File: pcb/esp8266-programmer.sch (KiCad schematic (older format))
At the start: 9 parts, among them P1 USB_OTG, P2 CONN_01X04, SW1 RESET, SW2 FLASH, SW3 SW_DP3T, U1 AP1117

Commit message: Edit Kicad schematic to add basic components
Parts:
- added JP1: Jumper_NO_Dual, symbol Jumper_NO_Dual
- added R1, R2, R3, R?: R, symbol R
- gave numbers to parts that had none: 1
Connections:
- net labels added: PP_CH_EN, PP_GPIO0, PP_GPIO15, PP_GPIO2, PP_REST, VCC
- wire segments 18 -> 32
- no-connect marks 2 -> 3
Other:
- moved on the sheet: SW1, SW2, SW3B
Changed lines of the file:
@@
 LIBS:switches
 LIBS:sw_dp3t
+LIBS:jumper_no_dual
 LIBS:esp8266-programmer-cache
 EELAYER 25 0
@@
 L SW_Push_Dual SW2
 U 1 1 58DAC3C7
-P 4450 3450
-F 0 "SW2" H 4500 3550 50  0000 L CNN
-F 1 "FLASH" H 4450 3180 50  0000 C CNN
-F 2 "" H 4450 3650 50  0000 C CNN
-F 3 "" H 4450 3650 50  0000 C CNN
-	1    4450 3450
-	1    0    0    -1
+P 3650 3050
+F 0 "SW2" H 3700 3150 50  0000 L CNN
+F 1 "FLASH" H 3650 2780 50  0000 C CNN
+F 2 "" H 3650 3250 50  0000 C CNN
+F 3 "" H 3650 3250 50  0000 C CNN
+	1    3650 3050
+	-1   0    0    -1
 $EndComp
 $Comp
 L SW_Push_Dual SW1
 U 1 1 58DAC45A
-P 4450 2750
-F 0 "SW1" H 4500 2850 50  0000 L CNN
-F 1 "RESET" H 4450 2480 50  0000 C CNN
-F 2 "" H 4450 2950 50  0000 C CNN
-F 3 "" H 4450 2950 50  0000 C CNN
-	1    4450 2750
+P 1300 1650
+F 0 "SW1" H 1350 1750 50  0000 L CNN
+F 1 "RESET" H 1300 1380 50  0000 C CNN
+F 2 "" H 1300 1850 50  0000 C CNN
+F 3 "" H 1300 1850 50  0000 C CNN
+	1    1300 1650
 	1    0    0    -1
 $EndComp
@@
 NoConn ~ 8850 2450
 $Comp
-L SW_DP3T SW?
+L SW_DP3T SW3
 U 2 1 58DC1770
-P 5800 2550
-F 0 "SW?" H 5800 2750 50  0000 C CNN
-F 1 "SW_DP3T" H 5800 2350 50  0000 C CNN
-F 2 "" H 5175 2725 50  0000 C CNN
-F 3 "" H 5175 2725 50  0000 C CNN
-	2    5800 2550
+P 5800 2050
+F 0 "SW3" H 5800 2250 50  0000 C CNN
+F 1 "SW_DP3T" H 5800 1850 50  0000 C CNN
+F 2 "" H 5175 2225 50  0000 C CNN
+F 3 "" H 5175 2225 50  0000 C CNN
+	2    5800 2050
 	1    0    0    -1
 $EndComp
@@
 	8550 2650 6000 2650
 Wire Wire Line
-	6000 2050 6350 2050
+	6000 1950 6350 1950
 Wire Wire Line
 	6650 2350 7150 2350
 Wire Wire Line
-	6000 2050 6000 2550
-Connection ~ 6000 2450
-Wire Wire Line
-	5600 2550 5600 2050
-Wire Wire Line
-	5600 2050 5300 2050
+	5050 2050 5600 2050
 $Comp
 L GND #PWR?
@@
 Wire Wire Line
 	5300 2350 5300 2400
+Wire Wire Line
+	6000 2650 6000 2150
+Wire Wire Line
+	6000 1950 6000 2050
+Connection ~ 6000 1950
+Wire Wire Line
+	6350 1950 6350 2050
+Connection ~ 5300 2050
+$Comp
+L VCC #PWR?
+U 1 1 58DECEB5
+P 5050 2050
+F 0 "#PWR?" H 5050 1900 50  0001 C CNN
+F 1 "VCC" H 5050 2200 50  0000 C CNN
+F 2 "" H 5050 2050 50  0000 C CNN
+F 3 "" H 5050 2050 50  0000 C CNN
+	1    5050 2050
+	1    0    0    -1
+$EndComp
+Wire Wire Line
+	1100 1500 1100 1850
+Connection ~ 1100 1650
+$Comp
+L R R1
+U 1 1 58DED73E
+P 1100 1350
+F 0 "R1" H 1200 1350 50  0000 C CNN
+F 1 "R" H 1100 1350 50  0000 C CNN
+F 2 "" V 1030 1350 50  0000 C CNN
+F 3 "" H 1100 1350 50  0000 C CNN
+	1    1100 1350
+	1    0    0    -1
+$EndComp
+$Comp
+L VCC #PWR?
+U 1 1 58DED85C
+P 1100 1200
+F 0 "#PWR?" H 1100 1050 50  0001 C CNN
+F 1 "VCC" H 1100 1350 50  0000 C CNN
+F 2 "" H 1100 1200 50  0000 C CNN
+F 3 "" H 1100 1200 50  0000 C CNN
+	1    1100 1200
+	1    0    0    -1
+$EndComp
+Wire Wire Line
+	1500 1650 1500 1850
+Wire Wire Line
+	1500 1850 1950 1850
+Connection ~ 1500 1850
+Text Label 1800 1800 0    60   ~ 0
+PP_REST
+Wire Wire Line
+	3850 2900 3850 3250
+Connection ~ 3850 3050
+$Comp
+L R R3
+U 1 1 58DEDCA6
+P 3850 2750
+F 0 "R3" H 3950 2750 50  0000 C CNN
+F 1 "R" H 3850 2750 50  0000 C CNN
+F 2 "" V 3780 2750 50  0000 C CNN
+F 3 "" H 3850 2750 50  0000 C CNN
+	1    3850 2750
+	-1   0    0    -1
+$EndComp
+$Comp
+L VCC #PWR?
+U 1 1 58DEDE0F
+P 3850 2600
+F 0 "#PWR?" H 3850 2450 50  0001 C CNN
+F 1 "VCC" H 3850 2750 50  0000 C CNN
+F 2 "" H 3850 2600 50  0000 C CNN
+F 3 "" H 3850 2600 50  0000 C CNN
+	1    3850 2600
+	-1   0    0    -1
+$EndComp
+Wire Wire Line
+	3450 3050 3450 3250
+Wire Wire Line
+	3450 3250 3150 3250
+Connection ~ 3450 3250
+Text Label 3350 3200 2    60   ~ 0
+PP_GPIO0
+$Comp
+L VCC #PWR?
+U 1 1 58DEDF75
+P 1100 2800
+F 0 "#PWR?" H 1100 2650 50  0001 C CNN
+F 1 "VCC" H 1100 2950 50  0000 C CNN
+F 2 "" H 1100 2800 50  0000 C CNN
+F 3 "" H 1100 2800 50  0000 C CNN
+	1    1100 2800
+	1    0    0    -1
+$EndComp
+$Comp
+L R R2
+U 1 1 58DEDF9F
+P 1100 2950
+F 0 "R2" H 1200 2950 50  0000 C CNN
+F 1 "R" H 1100 2950 50  0000 C CNN
+F 2 "" V 1030 2950 50  0000 C CNN
+F 3 "" H 1100 2950 50  0000 C CNN
+	1    1100 2950
+	1    0    0    -1
+$EndComp
+Wire Wire Line
+	1100 3100 1100 3250
+Wire Wire Line
+	1100 3250 1950 3250
+Text Label 1750 3200 0    60   ~ 0
+PP_CH_EN
+$Comp
+L VCC #PWR?
+U 1 1 58DEEB71
+P 3850 4050
+F 0 "#PWR?" H 3850 3900 50  0001 C CNN
+F 1 "VCC" H 3850 4200 50  0000 C CNN
+F 2 "" H 3850 4050 50  0000 C CNN
+F 3 "" H 3850 4050 50  0000 C CNN
+	1    3850 4050
+	-1   0    0    -1
+$EndComp
+$Comp
+L R R?
+U 1 1 58DEEB77
+P 3850 4200
+F 0 "R?" V 3930 4200 50  0000 C CNN
+F 1 "R" V 3850 4200 50  0000 C CNN
+F 2 "" V 3780 4200 50  0000 C CNN
+F 3 "" H 3850 4200 50  0000 C CNN
+	1    3850 4200
+	-1   0    0    -1
+$EndComp
+Wire Wire Line
+	3850 4350 3850 4500
+Wire Wire Line
+	3850 4500 3150 4500
+Text Label 3350 4450 2    60   ~ 0
+PP_GPIO2
+$Comp
+L Jumper_NO_Dual JP1
+U 1 1 58DEE706
+P 1600 2100
+F 0 "JP1" V 1700 1850 50  0000 L CNN
+F 1 "Jumper_NO_Dual" V 1700 2550 50  0000 C BNN
+F 2 "" H 1600 2100 50  0000 C CNN
+F 3 "" H 1600 2100 50  0000 C CNN
+	1    1600 2100
+	0    -1   1    0
+$EndComp
+Wire Wire Line
+	1700 2100 1950 2100
+Text Label 1800 2050 0    60   ~ 0
+PP_REST
+NoConn ~ 1600 2350
+Wire Wire Line
+	3150 4850 3850 4850
+Wire Wire Line
+	3850 4850 3850 4950
+$Comp
+L GND #PWR?
+U 1 1 58DEF6C2
+P 3850 4950
+F 0 "#PWR?" H 3850 4700 50  0001 C CNN
+F 1 "GND" H 3850 4800 50  0000 C CNN
+F 2 "" H 3850 4950 50  0000 C CNN
+F 3 "" H 3850 4950 50  0000 C CNN
+	1    3850 4950
+	1    0    0    -1
+$EndComp
+Text Label 3350 4800 2    60   ~ 0
+PP_GPIO15
 $EndSCHEMATC

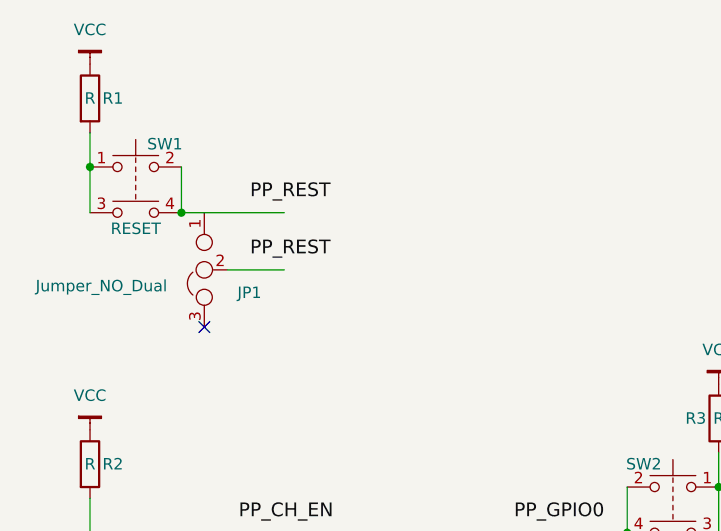
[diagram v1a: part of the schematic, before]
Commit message: Edit Kicad schematic to add basic components (again)
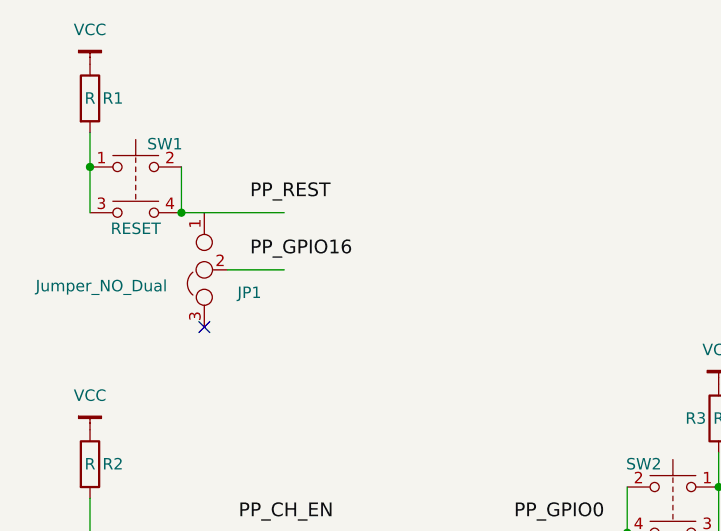
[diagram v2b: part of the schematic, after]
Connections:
- net labels added: PP_GPIO16
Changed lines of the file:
@@
 	1700 2100 1950 2100
 Text Label 1800 2050 0    60   ~ 0
-PP_REST
+PP_GPIO16
 NoConn ~ 1600 2350
 Wire Wire Line

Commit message: Add ESP chip, USB chip and some pin designations
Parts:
- added U?: ESP-12, symbol ESP-12
- added U?: MCP2221-I/SL, IPC7351-Nominal:SOIC127P600X175-14, symbol MCP2221-I/SL
- P1: symbol USB_OTG -> USB_OTG-RESCUE-esp8266-programmer
- U1: symbol AP1117 -> AP1117-RESCUE-esp8266-programmer
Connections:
- net labels added: D+, D-, PP_ADC, PP_GPIO12, PP_GPIO13, PP_GPIO14, PP_GPIO4, PP_GPIO5, PP_RXD, PP_TXD
- wire segments 32 -> 53
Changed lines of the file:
@@
 EESchema Schematic File Version 2
+LIBS:esp8266-programmer-rescue
 LIBS:power
 LIBS:device
@@
 LIBS:valves
 LIBS:switches
-LIBS:sw_dp3t
-LIBS:jumper_no_dual
+LIBS:ESP8266
+LIBS:Microchip
 LIBS:esp8266-programmer-cache
 EELAYER 25 0
@@
 $EndDescr
 $Comp
-L USB_OTG P1
+L USB_OTG-RESCUE-esp8266-programmer P1
 U 1 1 58DABF08
 P 9150 1650
@@
 $EndComp
 $Comp
-L AP1117 U1
+L AP1117-RESCUE-esp8266-programmer U1
 U 1 1 58DC158E
 P 6650 2050
@@
 Text Label 3350 4800 2    60   ~ 0
 PP_GPIO15
+$Comp
+L ESP-12 U?
+U 1 1 58DFBEBA
+P 6450 4200
+F 0 "U?" H 6450 4100 50  0000 C CNN
+F 1 "ESP-12" H 6450 4300 50  0000 C CNN
+F 2 "" H 6450 4200 50  0001 C CNN
+F 3 "" H 6450 4200 50  0001 C CNN
+	1    6450 4200
+	1    0    0    -1
+$EndComp
+Wire Wire Line
+	5550 3900 5100 3900
+Text Label 5150 3900 0    60   ~ 0
+PP_REST
+Wire Wire Line
+	5550 4100 5100 4100
+Text Label 5150 4100 0    60   ~ 0
+PP_CH_EN
+Wire Wire Line
+	5550 4000 5100 4000
+Text Label 5150 4000 0    60   ~ 0
+PP_ADC
+Wire Wire Line
+	5550 4200 5100 4200
+Text Label 5150 4200 0    60   ~ 0
+PP_GPIO16
+Wire Wire Line
+	5550 4300 5100 4300
+Text Label 5150 4300 0    60   ~ 0
+PP_GPIO14
+Wire Wire Line
+	5550 4400 5100 4400
+Text Label 5150 4400 0    60   ~ 0
+PP_GPIO12
+Wire Wire Line
+	5550 4500 5100 4500
+Text Label 5150 4500 0    60   ~ 0
+PP_GPIO13
+Wire Wire Line
+	7350 4500 7800 4500
+Wire Wire Line
+	7350 4400 7800 4400
+Wire Wire Line
+	7350 4300 7800 4300
+Wire Wire Line
+	7350 4200 7800 4200
+Wire Wire Line
+	7350 4100 7800 4100
+Wire Wire Line
+	7350 4000 7800 4000
+Wire Wire Line
+	7350 3900 7800 3900
+Text Label 7300 3900 0    60   ~ 0
+PP_TXD
+Text Label 7300 4000 0    60   ~ 0
+PP_RXD
+Text Label 7300 4100 0    60   ~ 0
+PP_GPIO5
+Text Label 7300 4200 0    60   ~ 0
+PP_GPIO4
+Text Label 7300 4300 0    60   ~ 0
+PP_GPIO0
+Text Label 7300 4400 0    60   ~ 0
+PP_GPIO2
+Text Label 7300 4500 0    60   ~ 0
+PP_GPIO15
+$Comp
+L MCP2221-I/SL U?
+U 1 1 58DFCE15
+P 9150 4250
+F 0 "U?" H 9150 5100 50  0000 C CNN
+F 1 "MCP2221-I/SL" H 9150 5000 50  0000 C CNN
+F 2 "IPC7351-Nominal:SOIC127P600X175-14" H 9150 5000 60  0001 C CNN
+F 3 "http://ww1.microchip.com/downloads/en/DeviceDoc/20005292B.pdf" H 9150 5000 60  0001 C CNN
+F 4 "IC MICROCHIP MCP2221-I/SL" H 9650 5800 60  0001 C CNN "BOM"
+	1    9150 4250
+	1    0    0    -1
+$EndComp
+Wire Wire Line
+	8550 3650 8450 3650
+Wire Wire Line
+	8450 3650 8450 3350
+$Comp
+L VCC #PWR?
+U 1 1 58DFD4A9
+P 8450 3350
+F 0 "#PWR?" H 8450 3400 30  0001 C CNN
+F 1 "VCC" H 8450 3450 50  0000 C CNN
+F 2 "" H 8450 3350 60  0000 C CNN
+F 3 "" H 8450 3350 60  0000 C CNN
+	1    8450 3350
+	1    0    0    -1
+$EndComp
+$Comp
+L VCC #PWR?
+U 1 1 58DFD4DD
+P 6450 3300
+F 0 "#PWR?" H 6450 3350 30  0001 C CNN
+F 1 "VCC" H 6450 3400 50  0000 C CNN
+F 2 "" H 6450 3300 60  0000 C CNN
+F 3 "" H 6450 3300 60  0000 C CNN
+	1    6450 3300
+	1    0    0    -1
+$EndComp
+$Comp
+L GND #PWR?
+U 1 1 58DFD60B
+P 8550 5350
+F 0 "#PWR?" H 8550 5350 30  0001 C CNN
+F 1 "GND" H 8550 5280 30  0001 C CNN
+F 2 "" H 8550 5350 60  0000 C CNN
+F 3 "" H 8550 5350 60  0000 C CNN
+	1    8550 5350
+	1    0    0    -1
+$EndComp
+Wire Wire Line
+	8550 4850 8550 5350
+Wire Wire Line
+	8850 1550 8500 1550
+Wire Wire Line
+	8850 1650 8500 1650
+Text Label 8600 1550 0    60   ~ 0
+D-
+Text Label 8600 1650 0    60   ~ 0
+D+
+Wire Wire Line
+	8550 4150 8400 4150
+Wire Wire Line
+	8550 4250 8400 4250
+Text Label 8450 4250 0    60   ~ 0
+D+
+Text Label 8450 4150 0    60   ~ 0
+D-
 $EndSCHEMATC

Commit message: Add custom Kicad libs directory to project directory
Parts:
- removed U1: AP1117, TO_SOT_Packages_SMD:SOT-223, symbol AP1117-RESCUE-esp8266-programmer
- added U1: MCP1700T-3302E/TT, KiCad/TO_SOT_Packages_SMD.pretty:SOT-23, symbol MCP1700T-3302E/TT
- gave numbers to parts that had none: 2
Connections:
- wire segments 53 -> 50
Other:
- moved on the sheet: C2, SW3B
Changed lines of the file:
@@
 LIBS:valves
 LIBS:switches
-LIBS:ESP8266
-LIBS:Microchip
+LIBS:mcp1700
+LIBS:jumper_no_dual
 LIBS:esp8266-programmer-cache
 EELAYER 25 0
@@
 $EndDescr
 $Comp
-L USB_OTG-RESCUE-esp8266-programmer P1
-U 1 1 58DABF08
-P 9150 1650
-F 0 "P1" V 8800 1650 50  0000 C CNN
-F 1 "USB_OTG" V 9150 2050 50  0000 C CNN
-F 2 "" V 9100 1550 50  0000 C CNN
-F 3 "" V 9100 1550 50  0000 C CNN
-	1    9150 1650
-	0    1    1    0
-$EndComp
-$Comp
 L SW_Push_Dual SW2
 U 1 1 58DAC3C7
@@
 $EndComp
 $Comp
-L GND #PWR01
-U 1 1 58DACFCE
-P 8850 1900
-F 0 "#PWR01" H 8850 1650 50  0001 C CNN
-F 1 "GND" H 8850 1750 50  0000 C CNN
-F 2 "" H 8850 1900 50  0000 C CNN
-F 3 "" H 8850 1900 50  0000 C CNN
-	1    8850 1900
-	1    0    0    -1
-$EndComp
-$Comp
-L GND #PWR02
-U 1 1 58DACFEE
-P 8850 2600
-F 0 "#PWR02" H 8850 2350 50  0001 C CNN
-F 1 "GND" H 8850 2450 50  0000 C CNN
-F 2 "" H 8850 2600 50  0000 C CNN
-F 3 "" H 8850 2600 50  0000 C CNN
-	1    8850 2600
-	1    0    0    -1
-$EndComp
-$Comp
 L SW_DP3T SW3
 U 1 1 58DC0605
 P 7650 2050
 F 0 "SW3" H 7650 2250 50  0000 C CNN
-F 1 "SW_DP3T" H 7650 1850 50  0000 C CNN
+F 1 "SW_DP3T" H 7600 1850 50  0000 C CNN
 F 2 "" H 7025 2225 50  0000 C CNN
 F 3 "" H 7025 2225 50  0000 C CNN
@@
 L CP C2
 U 1 1 58DC1487
-P 5300 2200
-F 0 "C2" H 5325 2300 50  0000 L CNN
-F 1 "CP" H 5325 2100 50  0000 L CNN
-F 2 "" H 5338 2050 50  0000 C CNN
-F 3 "" H 5300 2200 50  0000 C CNN
-	1    5300 2200
-	1    0    0    -1
-$EndComp
-$Comp
-L AP1117-RESCUE-esp8266-programmer U1
-U 1 1 58DC158E
-P 6650 2050
-F 0 "U1" H 6950 2250 50  0000 C CNN
-F 1 "AP1117" H 6650 2300 50  0000 C CNN
-F 2 "TO_SOT_Packages_SMD:SOT-223" H 6650 1700 50  0001 C CNN
-F 3 "" H 6750 1800 50  0000 C CNN
-	1    6650 2050
-	-1   0    0    -1
+P 5300 2300
+F 0 "C2" H 5325 2400 50  0000 L CNN
+F 1 "CP" H 5325 2200 50  0000 L CNN
+F 2 "" H 5338 2150 50  0000 C CNN
+F 3 "" H 5300 2300 50  0000 C CNN
+	1    5300 2300
+	1    0    0    -1
 $EndComp
 NoConn ~ 7850 2150
@@
 L SW_DP3T SW3
 U 2 1 58DC1770
-P 5800 2050
-F 0 "SW3" H 5800 2250 50  0000 C CNN
-F 1 "SW_DP3T" H 5800 1850 50  0000 C CNN
-F 2 "" H 5175 2225 50  0000 C CNN
-F 3 "" H 5175 2225 50  0000 C CNN
-	2    5800 2050
-	1    0    0    -1
-$EndComp
-$Comp
-L GND #PWR?
-U 1 1 58DC1DFC
-P 6900 2350
-F 0 "#PWR?" H 6900 2100 50  0001 C CNN
-F 1 "GND" H 6900 2200 50  0000 C CNN
-F 2 "" H 6900 2350 50  0000 C CNN
-F 3 "" H 6900 2350 50  0000 C CNN
-	1    6900 2350
+P 5800 2150
+F 0 "SW3" H 5800 2350 50  0000 C CNN
+F 1 "SW_DP3T" H 5750 1950 50  0000 C CNN
+F 2 "" H 5175 2325 50  0000 C CNN
+F 3 "" H 5175 2325 50  0000 C CNN
+	2    5800 2150
 	1    0    0    -1
 $EndComp
 Wire Wire Line
 	8100 1450 8850 1450
-Wire Wire Line
-	8850 1850 8850 2050
-Wire Wire Line
-	8850 2550 8850 2700
 Wire Wire Line
 	8100 1450 8100 1950
@@
 	8550 2650 6000 2650
 Wire Wire Line
-	6000 1950 6350 1950
+	6000 2050 6350 2050
 Wire Wire Line
 	6650 2350 7150 2350
 Wire Wire Line
-	5050 2050 5600 2050
-$Comp
-L GND #PWR?
+	5050 2150 5600 2150
+$Comp
+L GND-RESCUE-esp8266-programmer #PWR?
 U 1 1 58DC270D
-P 5300 2400
-F 0 "#PWR?" H 5300 2150 50  0001 C CNN
-F 1 "GND" H 5300 2250 50  0000 C CNN
-F 2 "" H 5300 2400 50  0000 C CNN
-F 3 "" H 5300 2400 50  0000 C CNN
-	1    5300 2400
-	1    0    0    -1
-$EndComp
-Wire Wire Line
-	5300 2350 5300 2400
-Wire Wire Line
-	6000 2650 6000 2150
-Wire Wire Line
-	6000 1950 6000 2050
-Connection ~ 6000 1950
-Wire Wire Line
-	6350 1950 6350 2050
-Connection ~ 5300 2050
-$Comp
-L VCC #PWR?
-U 1 1 58DECEB5
-P 5050 2050
-F 0 "#PWR?" H 5050 1900 50  0001 C CNN
-F 1 "VCC" H 5050 2200 50  0000 C CNN
-F 2 "" H 5050 2050 50  0000 C CNN
-F 3 "" H 5050 2050 50  0000 C CNN
-	1    5050 2050
-	1    0    0    -1
-$EndComp
+P 5300 2500
+F 0 "#PWR?" H 5300 2250 50  0001 C CNN
+F 1 "GND" H 5300 2400 50  0000 C CNN
+F 2 "" H 5300 2500 50  0000 C CNN
+F 3 "" H 5300 2500 50  0000 C CNN
+	1    5300 2500
+	1    0    0    -1
+$EndComp
+Wire Wire Line
+	5300 2450 5300 2500
+Wire Wire Line
+	6000 2650 6000 2250
+Wire Wire Line
+	6000 2050 6000 2150
+Connection ~ 6000 2050
+Connection ~ 5300 2150
 Wire Wire Line
 	1100 1500 1100 1850
@@
 $EndComp
 $Comp
-L R R?
+L R R4
 U 1 1 58DEEB77
 P 3850 4200
-F 0 "R?" V 3930 4200 50  0000 C CNN
-F 1 "R" V 3850 4200 50  0000 C CNN
+F 0 "R4" H 3950 4200 50  0000 C CNN
+F 1 "R" H 3850 4200 50  0000 C CNN
 F 2 "" V 3780 4200 50  0000 C CNN
 F 3 "" H 3850 4200 50  0000 C CNN
@@
 	3850 4850 3850 4950
 $Comp
-L GND #PWR?
+L GND-RESCUE-esp8266-programmer #PWR?
 U 1 1 58DEF6C2
 P 3850 4950
 F 0 "#PWR?" H 3850 4700 50  0001 C CNN
-F 1 "GND" H 3850 4800 50  0000 C CNN
+F 1 "GND" H 3850 4850 50  0000 C CNN
 F 2 "" H 3850 4950 50  0000 C CNN
 F 3 "" H 3850 4950 50  0000 C CNN
@@
 PP_GPIO15
 $Comp
-L MCP2221-I/SL U?
+L MCP2221-I/SL U1
 U 1 1 58DFCE15
 P 9150 4250
-F 0 "U?" H 9150 5100 50  0000 C CNN
+F 0 "U1" H 9150 5100 50  0000 C CNN
 F 1 "MCP2221-I/SL" H 9150 5000 50  0000 C CNN
 F 2 "IPC7351-Nominal:SOIC127P600X175-14" H 9150 5000 60  0001 C CNN
@@
 $EndComp
 Wire Wire Line
-	8550 3650 8450 3650
-Wire Wire Line
-	8450 3650 8450 3350
-$Comp
-L VCC #PWR?
-U 1 1 58DFD4A9
-P 8450 3350
-F 0 "#PWR?" H 8450 3400 30  0001 C CNN
-F 1 "VCC" H 8450 3450 50  0000 C CNN
-F 2 "" H 8450 3350 60  0000 C CNN
-F 3 "" H 8450 3350 60  0000 C CNN
-	1    8450 3350
-	1    0    0    -1
-$EndComp
-$Comp
-L VCC #PWR?
-U 1 1 58DFD4DD
-P 6450 3300
-F 0 "#PWR?" H 6450 3350 30  0001 C CNN
-F 1 "VCC" H 6450 3400 50  0000 C CNN
-F 2 "" H 6450 3300 60  0000 C CNN
-F 3 "" H 6450 3300 60  0000 C CNN
-	1    6450 3300
-	1    0    0    -1
-$EndComp
-$Comp
-L GND #PWR?
-U 1 1 58DFD60B
-P 8550 5350
-F 0 "#PWR?" H 8550 5350 30  0001 C CNN
-F 1 "GND" H 8550 5280 30  0001 C CNN
-F 2 "" H 8550 5350 60  0000 C CNN
-F 3 "" H 8550 5350 60  0000 C CNN
-	1    8550 5350
-	1    0    0    -1
-$EndComp
-Wire Wire Line
-	8550 4850 8550 5350
+	8550 3650 8550 3350
 Wire Wire Line
 	8850 1550 8500 1550
@@
 Text Label 8450 4150 0    60   ~ 0
 D-
+$Comp
+L GND #PWR?
+U 1 1 58E05ABF
+P 6900 2350
+F 0 "#PWR?" H 6900 2100 50  0001 C CNN
+F 1 "GND" H 6900 2200 50  0000 C CNN
+F 2 "" H 6900 2350 50  0000 C CNN
+F 3 "" H 6900 2350 50  0000 C CNN
+	1    6900 2350
+	1    0    0    -1
+$EndComp
+Connection ~ 6900 2350
+$Comp
+L USB_OTG-RESCUE-esp8266-programmer P1
+U 1 1 58DABF08
+P 9150 1650
+F 0 "P1" V 8850 1650 50  0000 C CNN
+F 1 "USB_OTG" V 9150 2050 50  0000 C CNN
+F 2 "" V 9100 1550 50  0000 C CNN
+F 3 "" V 9100 1550 50  0000 C CNN
+	1    9150 1650
+	0    1    1    0
+$EndComp
+$Comp
+L GND #PWR?
+U 1 1 58E05F00
+P 8850 1850
+F 0 "#PWR?" H 8850 1600 50  0001 C CNN
+F 1 "GND" H 8850 1700 50  0000 C CNN
+F 2 "" H 8850 1850 50  0000 C CNN
+F 3 "" H 8850 1850 50  0000 C CNN
+	1    8850 1850
+	1    0    0    -1
+$EndComp
+$Comp
+L GND #PWR?
+U 1 1 58E05FC7
+P 8850 2550
+F 0 "#PWR?" H 8850 2300 50  0001 C CNN
+F 1 "GND" H 8850 2400 50  0000 C CNN
+F 2 "" H 8850 2550 50  0000 C CNN
+F 3 "" H 8850 2550 50  0000 C CNN
+	1    8850 2550
+	1    0    0    -1
+$EndComp
+$Comp
+L VCC #PWR?
+U 1 1 58E06460
+P 8550 3350
+F 0 "#PWR?" H 8550 3200 50  0001 C CNN
+F 1 "VCC" H 8550 3500 50  0000 C CNN
+F 2 "" H 8550 3350 50  0000 C CNN
+F 3 "" H 8550 3350 50  0000 C CNN
+	1    8550 3350
+	1    0    0    -1
+$EndComp
+$Comp
+L GND #PWR?
+U 1 1 58E064F7
+P 8550 5000
+F 0 "#PWR?" H 8550 4750 50  0001 C CNN
+F 1 "GND" H 8550 4850 50  0000 C CNN
+F 2 "" H 8550 5000 50  0000 C CNN
+F 3 "" H 8550 5000 50  0000 C CNN
+	1    8550 5000
+	1    0    0    -1
+$EndComp
+Wire Wire Line
+	8550 4850 8550 5000
+$Comp
+L VCC #PWR?
+U 1 1 58E066ED
+P 6450 3300
+F 0 "#PWR?" H 6450 3150 50  0001 C CNN
+F 1 "VCC" H 6450 3450 50  0000 C CNN
+F 2 "" H 6450 3300 50  0000 C CNN
+F 3 "" H 6450 3300 50  0000 C CNN
+	1    6450 3300
+	1    0    0    -1
+$EndComp
+$Comp
+L GND #PWR?
+U 1 1 58E067DB
+P 6450 5100
+F 0 "#PWR?" H 6450 4850 50  0001 C CNN
+F 1 "GND" H 6450 4950 50  0000 C CNN
+F 2 "" H 6450 5100 50  0000 C CNN
+F 3 "" H 6450 5100 50  0000 C CNN
+	1    6450 5100
+	1    0    0    -1
+$EndComp
+$Comp
+L VCC #PWR?
+U 1 1 58E06D8F
+P 5050 2050
+F 0 "#PWR?" H 5050 1900 50  0001 C CNN
+F 1 "VCC" H 5050 2200 50  0000 C CNN
+F 2 "" H 5050 2050 50  0000 C CNN
+F 3 "" H 5050 2050 50  0000 C CNN
+	1    5050 2050
+	1    0    0    -1
+$EndComp
+Wire Wire Line
+	5050 2050 5050 2150
+$Comp
+L MCP1700T-3302E/TT U1
+U 1 1 58E084E7
+P 6650 2150
+F 0 "U1" H 6750 1950 50  0000 C CNN
+F 1 "MCP1700T-3302E/TT" H 6650 2450 50  0000 C CNN
+F 2 "KiCad/TO_SOT_Packages_SMD.pretty:SOT-23" H 6650 2250 50  0001 C CNN
+F 3 "http://docs-europe.electrocomponents.com/webdocs/0dd1/0900766b80dd189b.pdf" H 6650 2250 50  0001 C CNN
+	1    6650 2150
+	-1   0    0    -1
+$EndComp
 $EndSCHEMATC

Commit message: Create kicad_extras directory for libs, modules, 3d shapes. Move relevant files. Set relative paths for libs
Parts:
- U?: footprint (none) -> jdunmire/kicad-ESP8266/ESP8266.pretty:ESP-12
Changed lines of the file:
@@
 EESchema Schematic File Version 2
-LIBS:esp8266-programmer-rescue
 LIBS:power
 LIBS:device
@@
 LIBS:valves
 LIBS:switches
+LIBS:ESP8266
+LIBS:Microchip
 LIBS:mcp1700
 LIBS:jumper_no_dual
@@
 F 0 "U?" H 6450 4100 50  0000 C CNN
 F 1 "ESP-12" H 6450 4300 50  0000 C CNN
-F 2 "" H 6450 4200 50  0001 C CNN
+F 2 "jdunmire/kicad-ESP8266/ESP8266.pretty:ESP-12" H 6450 4200 50  0001 C CNN
 F 3 "" H 6450 4200 50  0001 C CNN
 	1    6450 4200
@@
 D-
 $Comp
-L GND #PWR?
+L GND-RESCUE-esp8266-programmer #PWR?
 U 1 1 58E05ABF
 P 6900 2350
@@
 $EndComp
 $Comp
-L GND #PWR?
+L GND-RESCUE-esp8266-programmer #PWR?
 U 1 1 58E05F00
 P 8850 1850
@@
 $EndComp
 $Comp
-L GND #PWR?
+L GND-RESCUE-esp8266-programmer #PWR?
 U 1 1 58E05FC7
 P 8850 2550
@@
 $EndComp
 $Comp
-L GND #PWR?
+L GND-RESCUE-esp8266-programmer #PWR?
 U 1 1 58E064F7
 P 8550 5000
@@
 $EndComp
 $Comp
-L GND #PWR?
+L GND-RESCUE-esp8266-programmer #PWR?
 U 1 1 58E067DB
 P 6450 5100
